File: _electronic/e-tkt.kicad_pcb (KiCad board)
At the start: 4 copper layers, 99.6 x 76.2 mm, 109 parts, among them J1 Conn_01x03_Pin, J2 Conn_01x03_Pin, J3 Conn_01x03_Pin, J4 USB_C_Receptacle_PowerOnly_6P, U1 HUSB237-AA001-DN06R

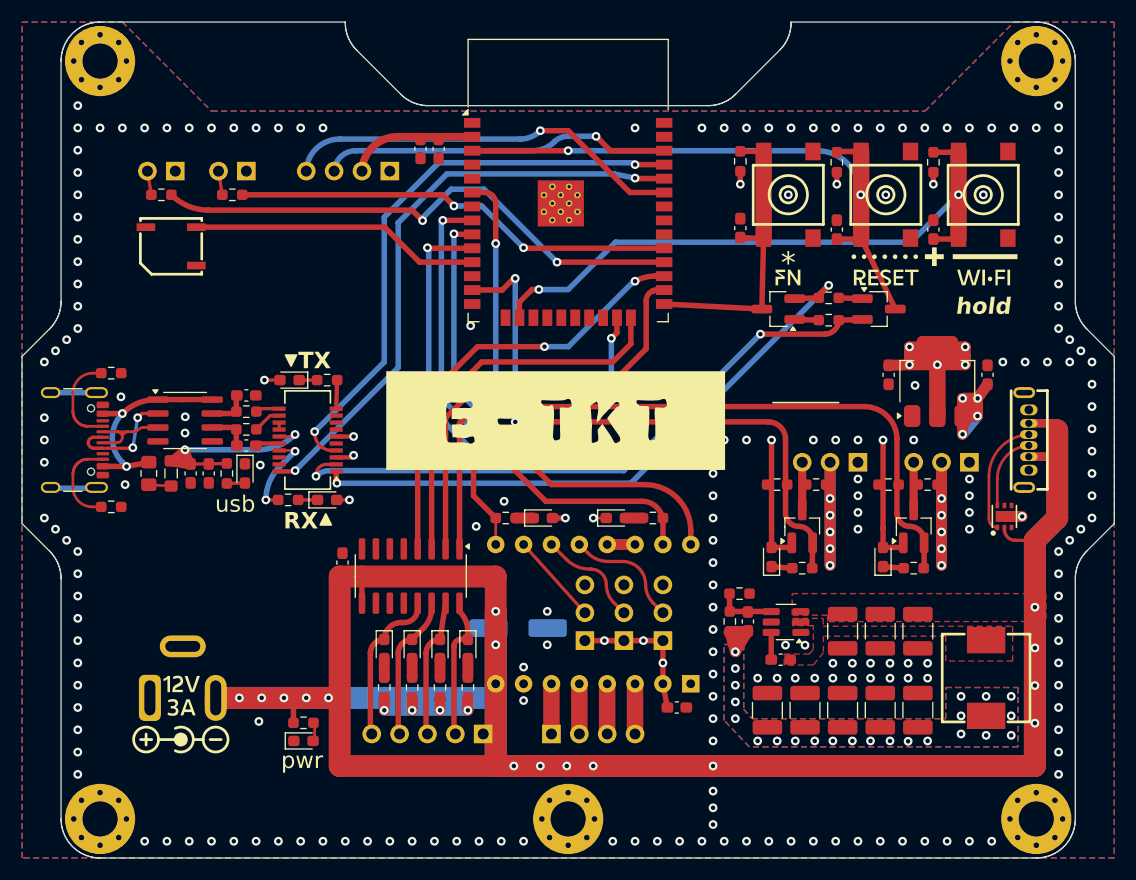
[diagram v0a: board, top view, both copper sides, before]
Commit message: Added endstop
added footprint for a microswitch with roller as enstop. updated the CAD correspondingly by adding M4 hole in the nema wheel hub for an M4 12mm/16mm set screw (the ones with a pointy end).
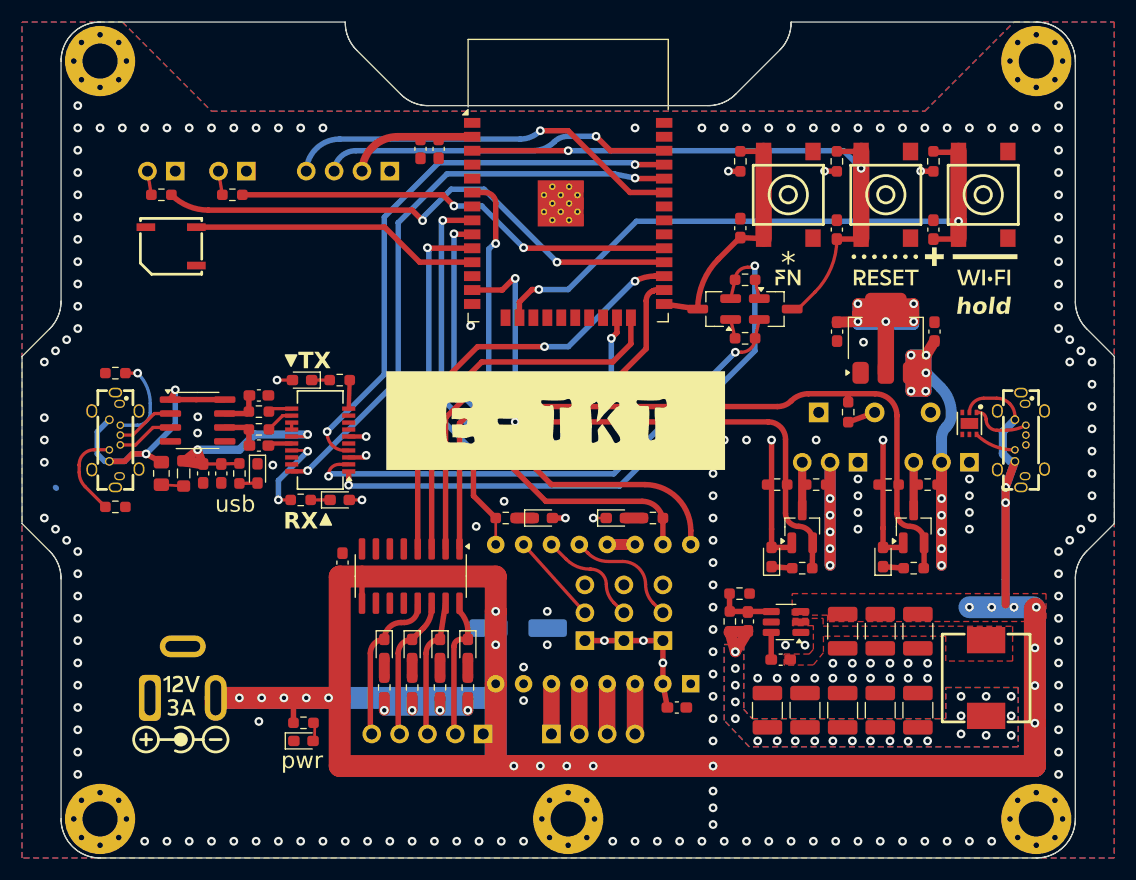
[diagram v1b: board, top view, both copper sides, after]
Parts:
- removed J4: USB_C_Receptacle_PowerOnly_6P, EASYEDA2KICAD:USB-C-TH_TYPE-604-T3-5A
- added J_USB2: USB_C_Receptacle_USB2.0_14P, EASYEDA2KICAD:USB-TH_GT-USB-7057A, F.Cu at (219.6, -189.5)
- added R_Endstop1: 100R, Resistor_SMD:R_0603_1608Metric_Pad0.98x0.95mm_HandSolder, F.Cu at (203.8, -192.0)
- added SW1: SW_SPDT, EASYEDA2KICAD:SW-TH_JL010, B.Cu at (206.2, -192.0)
- J_USB1: footprint Connector_USB:USB_C_Receptacle_GCT_USB4105-xx-A_16P_TopMnt_Horizontal -> EASYEDA2KICAD:USB-TH_GT-USB-7057A
- moved Q_AUTO1 9.40 mm to (197.2, -201.4)
- moved U1 9.06 mm to (214.9, -191.0), turned to -90 degrees
- moved R_AUTO1 7.80 mm to (194.4, -204.1)
- moved R_AUTO2 7.80 mm to (194.4, -198.8)
- moved C_POW1 6.23 mm to (211.7, -199.4)
- moved C_POW2 6.13 mm to (202.8, -199.4)
- moved U_POW2 6.13 mm to (207.3, -198.8)
- moved Q_AUTO2 5.84 mm to (191.6, -201.4)
- moved J_USB1 4.83 mm to (137.0, -189.5)
- moved C_SER2 1.14 mm to (150.1, -189.0)
- moved C_SER3 1.14 mm to (150.1, -193.5)
- moved C_SER4 1.14 mm to (145.0, -186.4)
- moved C_SER5 1.14 mm to (146.7, -186.4)
- moved D_RX1 1.14 mm to (157.5, -184.0)
- moved D_TX1 1.14 mm to (154.1, -194.9)
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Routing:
- net Net-(F_USB1-Pad1): track 19.0 -> 34.8 mm
- net RTS: track 58.4 -> 48.3 mm
- net +6V: track 59.9 -> 68.9 mm, vias 37 -> 38
- net +3.3V: track 83.0 -> 91.3 mm
- net +12V: track 308.5 -> 314.4 mm, vias 20 -> 25
- net Net-(J_USB2-CC1): track 10.9 -> 5.43 mm
- net Net-(J_USB1-D+-PadA6): track 9.94 -> 5.38 mm, vias 2 -> 0
- net IO0 DFU: track 28.1 -> 23.6 mm
- net Net-(J_USB2-CC2): track 7.09 -> 3.85 mm
- net IO34 HALL: track 72.5 -> 75.6 mm
- net Net-(SW1-B): track 0.00 -> 2.64 mm
- net GNDREF: track 15.4 -> 17.7 mm, vias 202 -> 190
- net Net-(J_USB1-D--PadA7): track 8.01 -> 6.12 mm
- net DTR: track 56.9 -> 55.2 mm
- net IO13 WIFI RST: track 57.9 -> 56.9 mm
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- added copper zone on In2.Cu, net +12V
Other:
- board text added: "Endstop"

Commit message: sturdify again
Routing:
- net DTR: track 55.2 -> 54.1 mm

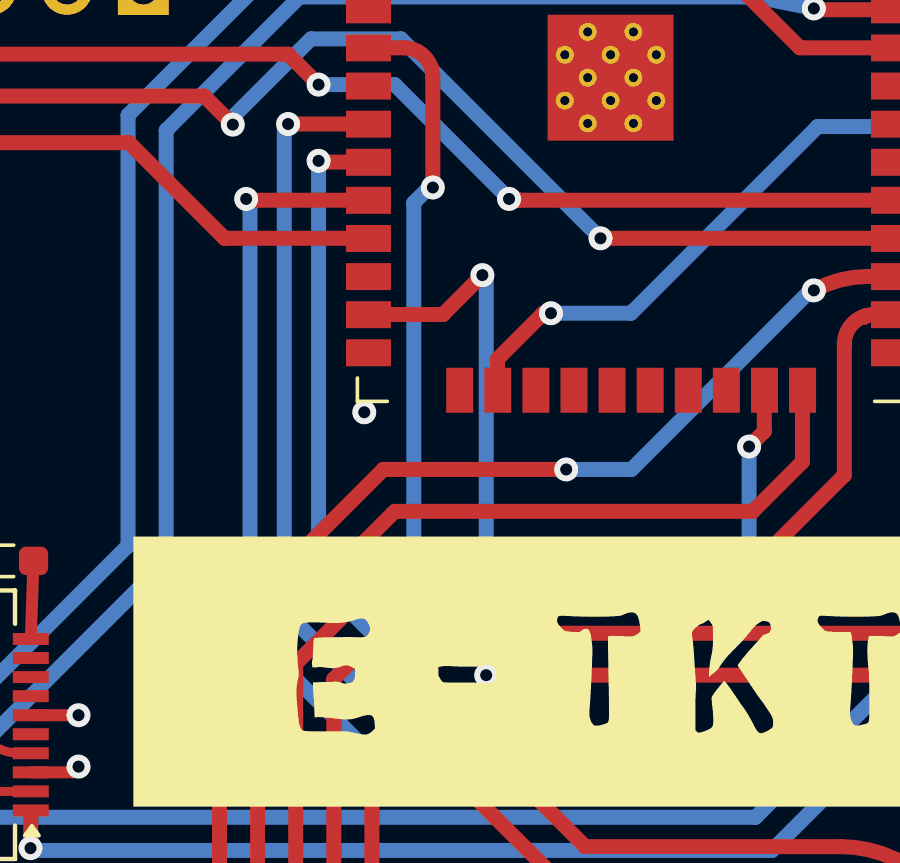
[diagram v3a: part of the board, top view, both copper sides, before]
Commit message: JLC export added, LCSC numbers updated
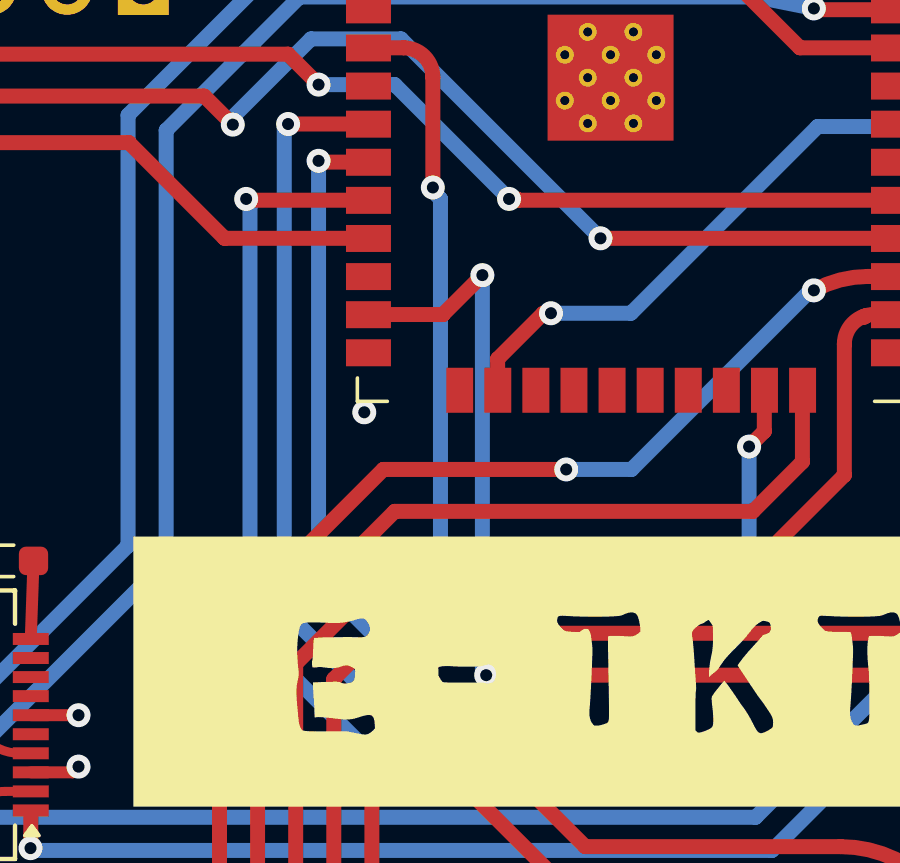
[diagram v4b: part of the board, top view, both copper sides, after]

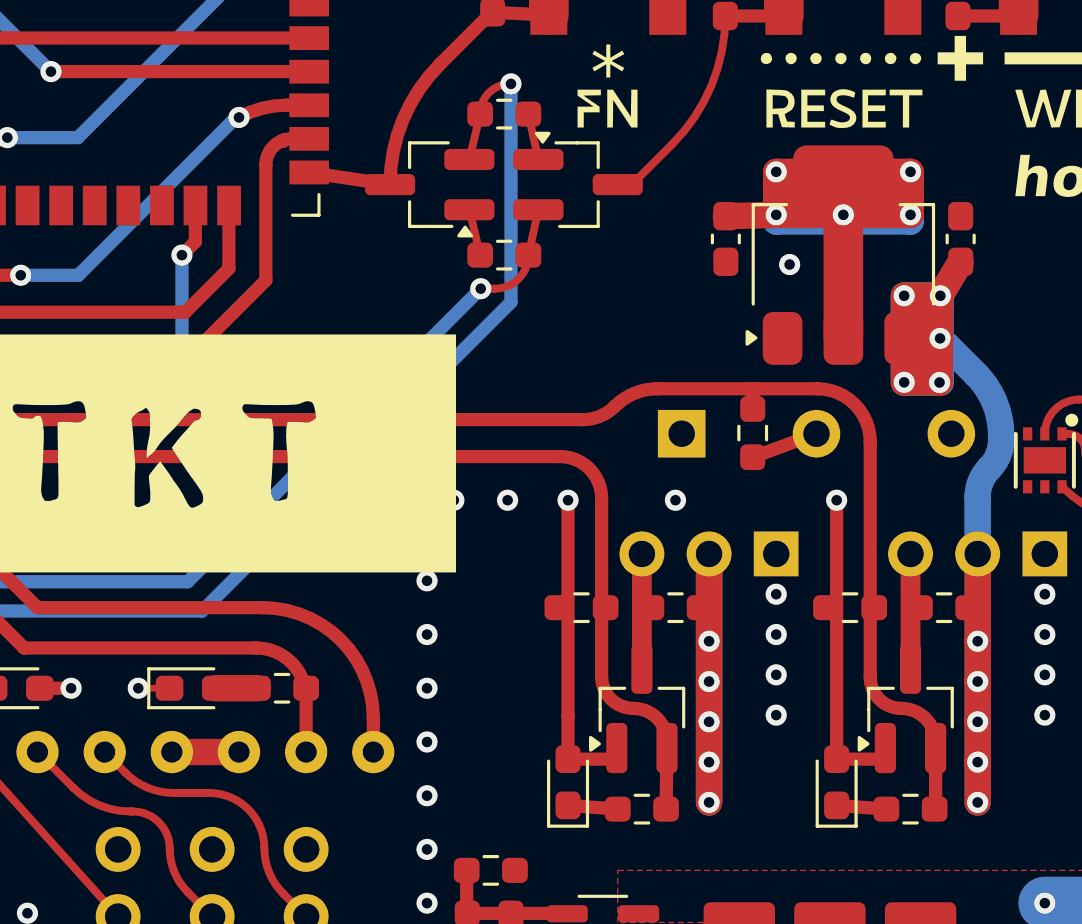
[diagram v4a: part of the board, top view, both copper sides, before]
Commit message: Updated layout of schematic symbol's text
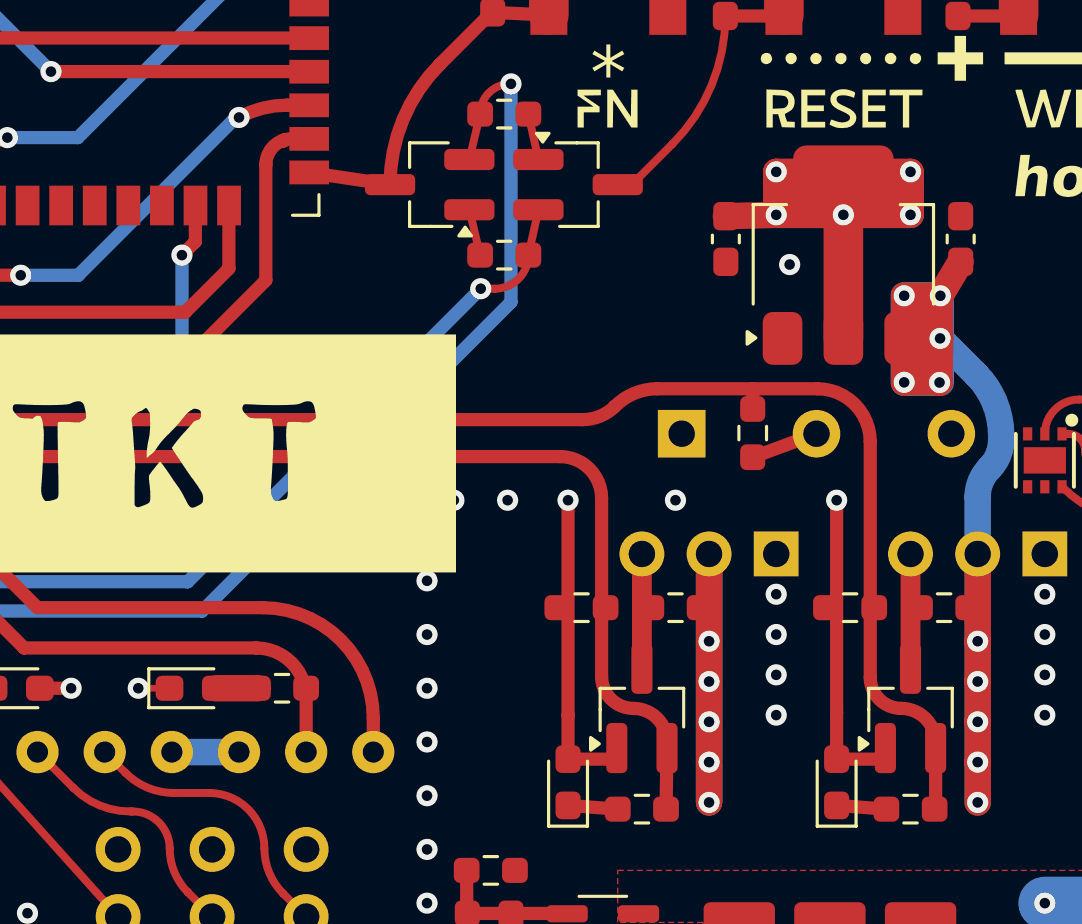
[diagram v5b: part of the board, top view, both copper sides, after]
